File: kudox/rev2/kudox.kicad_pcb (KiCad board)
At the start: 2 copper layers, 143.6 x 129.5 mm, 81 parts, among them K0 KEYSW, K1 KEYSW, K10 KEYSW, K11 KEYSW, K12 KEYSW, K13 KEYSW, K14 KEYSW, K15 KEYSW, K16 KEYSW, K2 KEYSW, K20 KEYSW, K21 KEYSW, K22 KEYSW, K23 KEYSW, K24 KEYSW, K25 KEYSW, K3 KEYSW, K30 KEYSW, K31 KEYSW, K32 KEYSW, K33 KEYSW, K34 KEYSW, K35 KEYSW, K4 KEYSW, K40 KEYSW, K41 KEYSW, K42 KEYSW, K43 KEYSW, K44 KEYSW, K45 KEYSW, K46 KEYSW, K5 KEYSW, U1 ProMicro

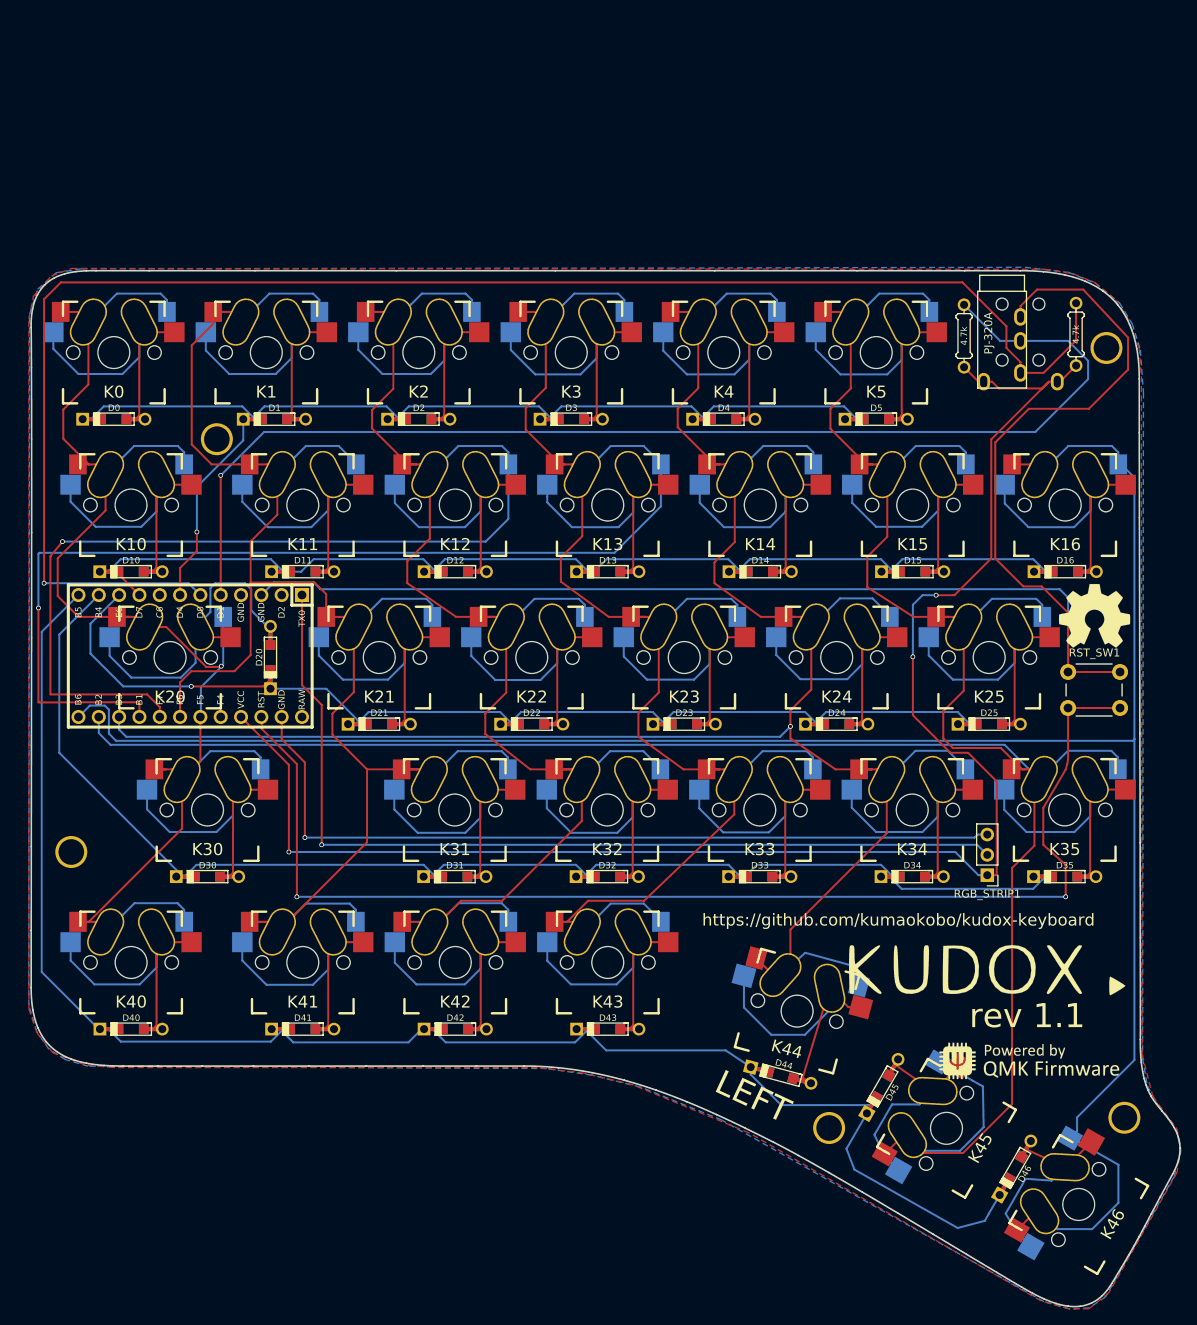
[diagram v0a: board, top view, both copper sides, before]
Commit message: Add more tracks.
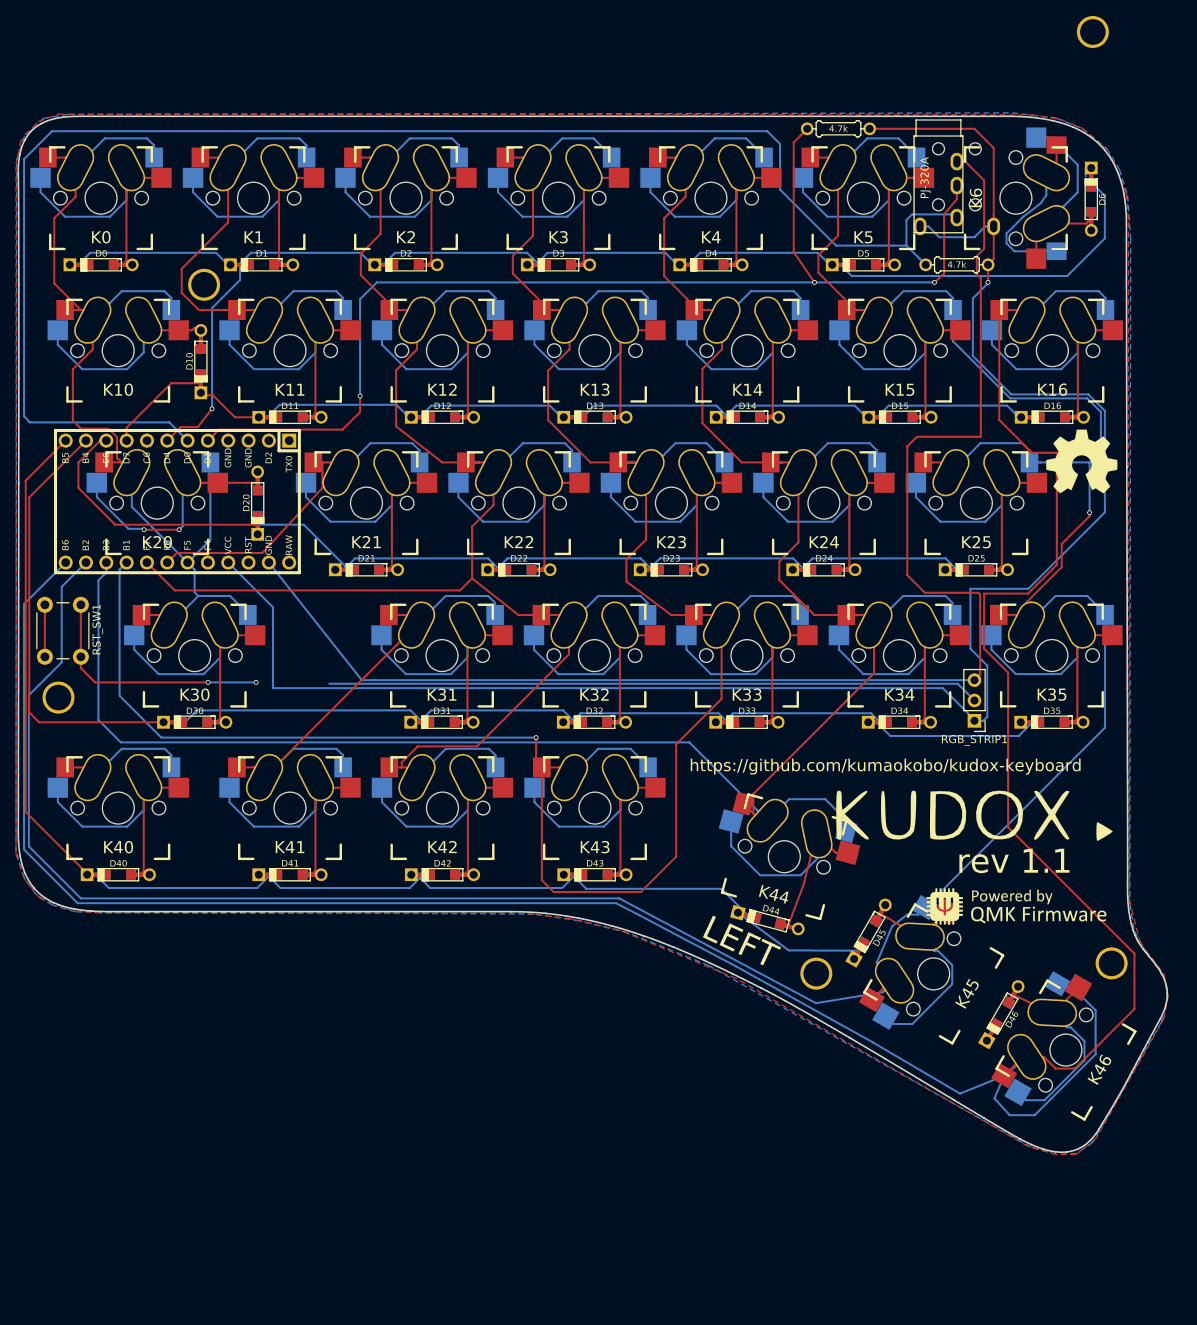
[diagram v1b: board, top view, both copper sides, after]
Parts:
- removed the G*** at (200.4, 138.2)
- removed the G*** at (201.3, 138.1)
- removed the G*** at (206.6, 149.5)
- removed the G*** at (206.8, 149.6)
- removed the HOLE_M3 at (181.5, 157.9)
- removed the HOLE_M3 at (218.4, 156.6)
- removed the HOLE_M3 at (105.0, 71.8)
- removed the HOLE_M3 at (86.8, 123.4)
- removed the HOLE_M3 at (216.2, 60.4)
- added D6: D, kudox_footprints:Diode-dual, F.Cu at (214.3, 41.8)
- added G***: LOGO, kudox_footprints:kudox-logo, B.Cu at (198.8, 118.9)
- added G***: LOGO, kudox_footprints:kudox-logo, F.Cu at (199.7, 118.8)
- added G***: LOGO, myparts:qmk-badge, F.Cu at (205.0, 130.2)
- added G***: LOGO, myparts:qmk-badge, B.Cu at (205.2, 130.3)
- added HOLE_M3: VAL**, keyboard_parts:HOLE_M3, F.Cu at (179.9, 138.6)
- added HOLE_M3: VAL**, keyboard_parts:HOLE_M3, F.Cu at (216.8, 137.3)
- added HOLE_M3: VAL**, keyboard_parts:HOLE_M3, F.Cu at (103.4, 52.5)
- added HOLE_M3: VAL**, keyboard_parts:HOLE_M3, F.Cu at (85.2, 104.1)
- added HOLE_M3: VAL**, keyboard_parts:HOLE_M3, F.Cu at (214.5, 20.9)
- added K6: KEYSW, kudox_footprints:Mx_hotswappable, F.Cu at (204.9, 41.6)
- moved RST_SW1 134.6 mm to (83.5, 99.0), turned to 90 degrees
- moved R1 30.3 mm to (182.7, 33.0), turned to 180 degrees
- moved D10 27.7 mm to (103.0, 62.1), turned to 270 degrees
- moved TRRS1 21.0 mm to (197.5, 33.9)
- moved D46 19.4 mm to (203.2, 143.6)
- moved K45 19.4 mm to (194.6, 138.6)
- moved RGB_STRIP1 19.4 mm to (199.7, 107.0)
- moved D0 19.4 mm to (90.5, 50.0)
- moved D1 19.4 mm to (110.6, 50.0)
- moved D2 19.4 mm to (128.6, 50.0)
- moved D3 19.4 mm to (147.7, 50.0)
- moved D4 19.4 mm to (166.8, 50.0)
- moved D5 19.4 mm to (185.8, 50.0)
- moved -3 19.4 mm to (213.1, 74.6)
- moved D11 19.4 mm to (114.1, 69.0)
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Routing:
- net RST: track 152.6 -> 6.50 mm, vias 2 -> 0
- net col6: track 269.6 -> 371.6 mm
- net GND: track 296.3 -> 209.8 mm, vias 1 -> 2
- net col2: track 289.1 -> 233.6 mm, vias 1 -> 0
- net col1: track 215.5 -> 167.1 mm
- net row0: track 138.8 -> 182.8 mm
- net rgb_data: track 116.0 -> 81.5 mm, vias 1 -> 0
- net VCC: track 202.7 -> 232.9 mm, vias 3 -> 1
- net col0: track 178.9 -> 149.8 mm, vias 1 -> 0
- net row4: track 202.2 -> 174.7 mm
- net Net-(D6-Pad2): track 0.00 -> 27.2 mm
- net col4: track 274.2 -> 298.1 mm, vias 1 -> 0
- net col5: track 351.0 -> 370.7 mm, vias 0 -> 1
- net row1: track 145.5 -> 134.0 mm
- net Net-(D20-Pad2): track 42.5 -> 31.1 mm, vias 0 -> 2
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
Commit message: Modified Mx hotswappable foot print.
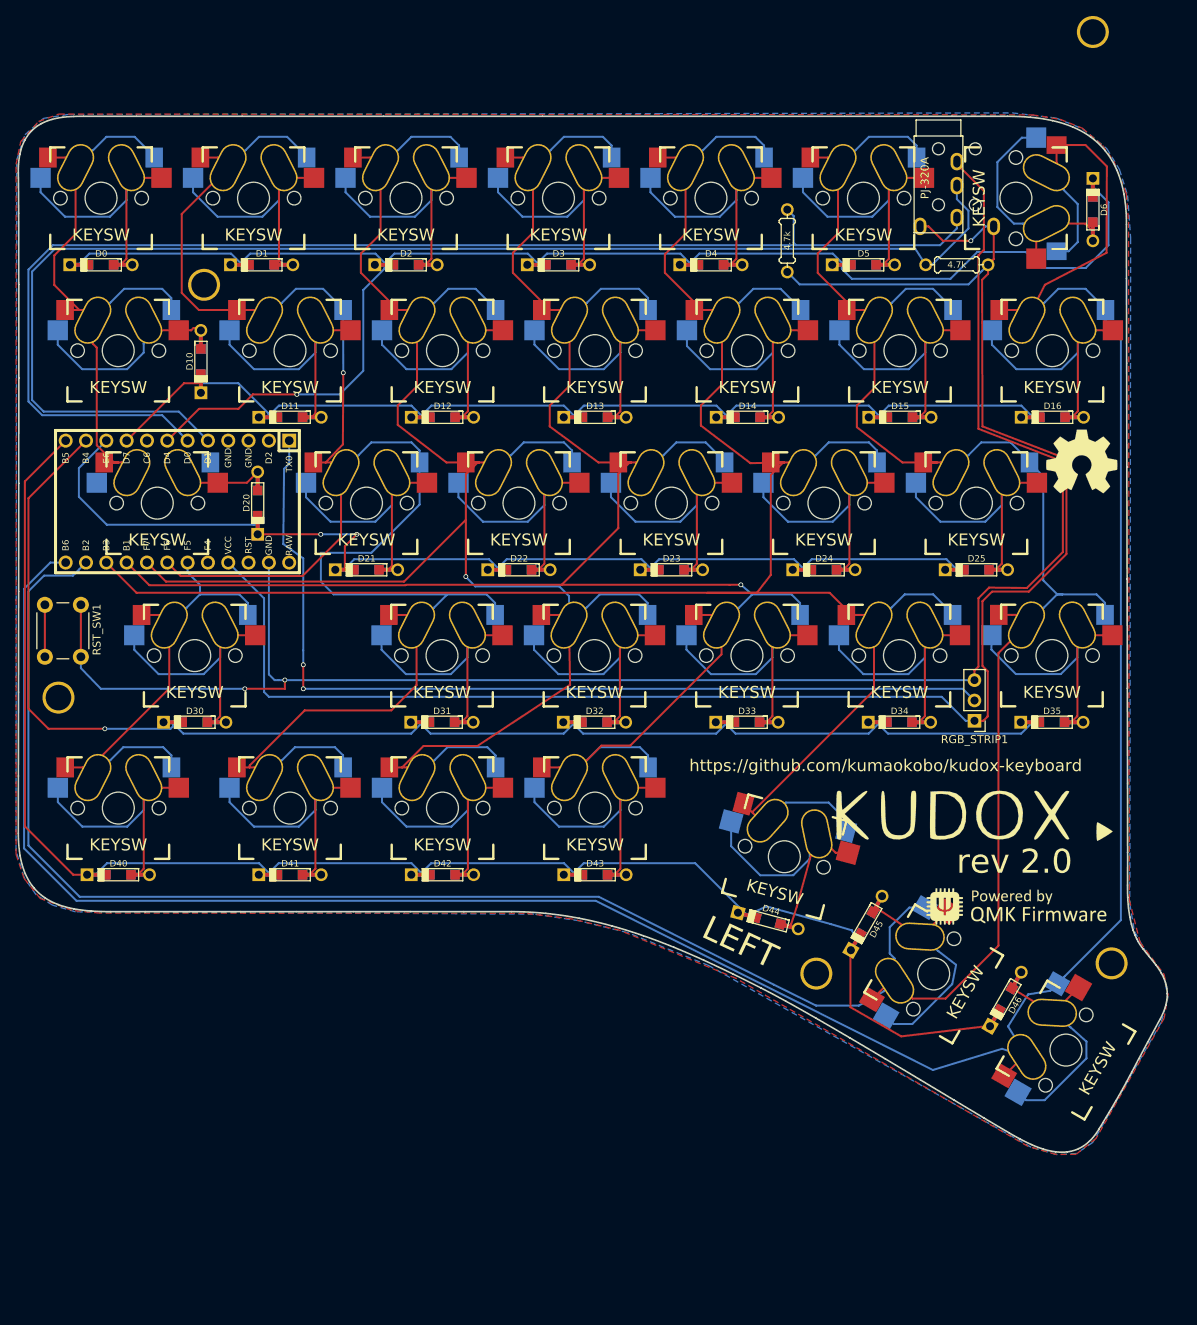
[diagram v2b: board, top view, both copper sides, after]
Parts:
- moved R1 22.5 mm to (197.5, 50.0)
- moved R2 21.4 mm to (176.3, 47.0), turned to 90 degrees
- moved D46 1.84 mm to (203.6, 141.8)
- moved D6 1.32 mm to (214.5, 43.1)
- moved D45 1.17 mm to (186.2, 132.3)
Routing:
- net col1: track 167.1 -> 237.8 mm, vias 0 -> 1
- net col3: track 297.5 -> 261.1 mm
- net rgb_data: track 81.5 -> 117.1 mm, vias 0 -> 2
- net row4: track 174.7 -> 202.6 mm
- net col6: track 371.6 -> 343.8 mm
- net SDA: track 141.2 -> 167.3 mm, vias 3 -> 0
- net SCL: track 188.2 -> 162.8 mm
- net Net-(D20-Pad2): track 31.1 -> 10.5 mm, vias 2 -> 0
- net row0: track 182.8 -> 202.1 mm
- net col4: track 298.1 -> 283.1 mm
- net col0: track 149.8 -> 139.9 mm
- net GND: track 209.8 -> 219.2 mm
- net VCC: track 232.9 -> 224.0 mm
- net col2: track 233.6 -> 241.3 mm, vias 0 -> 1
- net col5: track 370.7 -> 364.4 mm, vias 1 -> 0
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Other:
- board text added: "rev 2.0"
- board text removed: "rev 1.1"

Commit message: Commit on half way.
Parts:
- moved HOLE_M3 29.3 mm to (215.1, 50.2)
- moved R1 21.4 mm to (176.5, 46.1), turned to 90 degrees
- moved R2 19.3 mm to (157.0, 46.1)
- moved D5 6.08 mm to (191.9, 50.0)
- moved TRRS1 2.10 mm to (195.4, 34.0)
- moved D6 1.00 mm to (214.5, 42.1), turned to 270 degrees
- turned K5 to 90 degrees
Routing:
- net col0: track 139.9 -> 195.4 mm, vias 0 -> 3
- net VCC: track 224.0 -> 275.5 mm, vias 1 -> 0
- net RST: track 6.50 -> 40.0 mm, vias 0 -> 1
- net SCL: track 162.8 -> 192.2 mm
- net col1: track 237.8 -> 218.2 mm, vias 1 -> 2
- net Net-(D20-Pad2): track 10.5 -> 29.5 mm
- net col5: track 364.4 -> 355.3 mm
- net row0: track 202.1 -> 193.6 mm
- net col6: track 343.8 -> 348.3 mm
- net Net-(D5-Pad2): track 36.9 -> 32.5 mm
- net SDA: track 167.3 -> 171.6 mm
- net GND: track 219.2 -> 222.9 mm, vias 2 -> 4
- net Net-(D6-Pad2): track 29.8 -> 32.7 mm
- net row2: track 139.6 -> 136.8 mm, vias 2 -> 1
- net row1: track 135.7 -> 136.9 mm
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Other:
- outline, holes or cut-outs redrawn

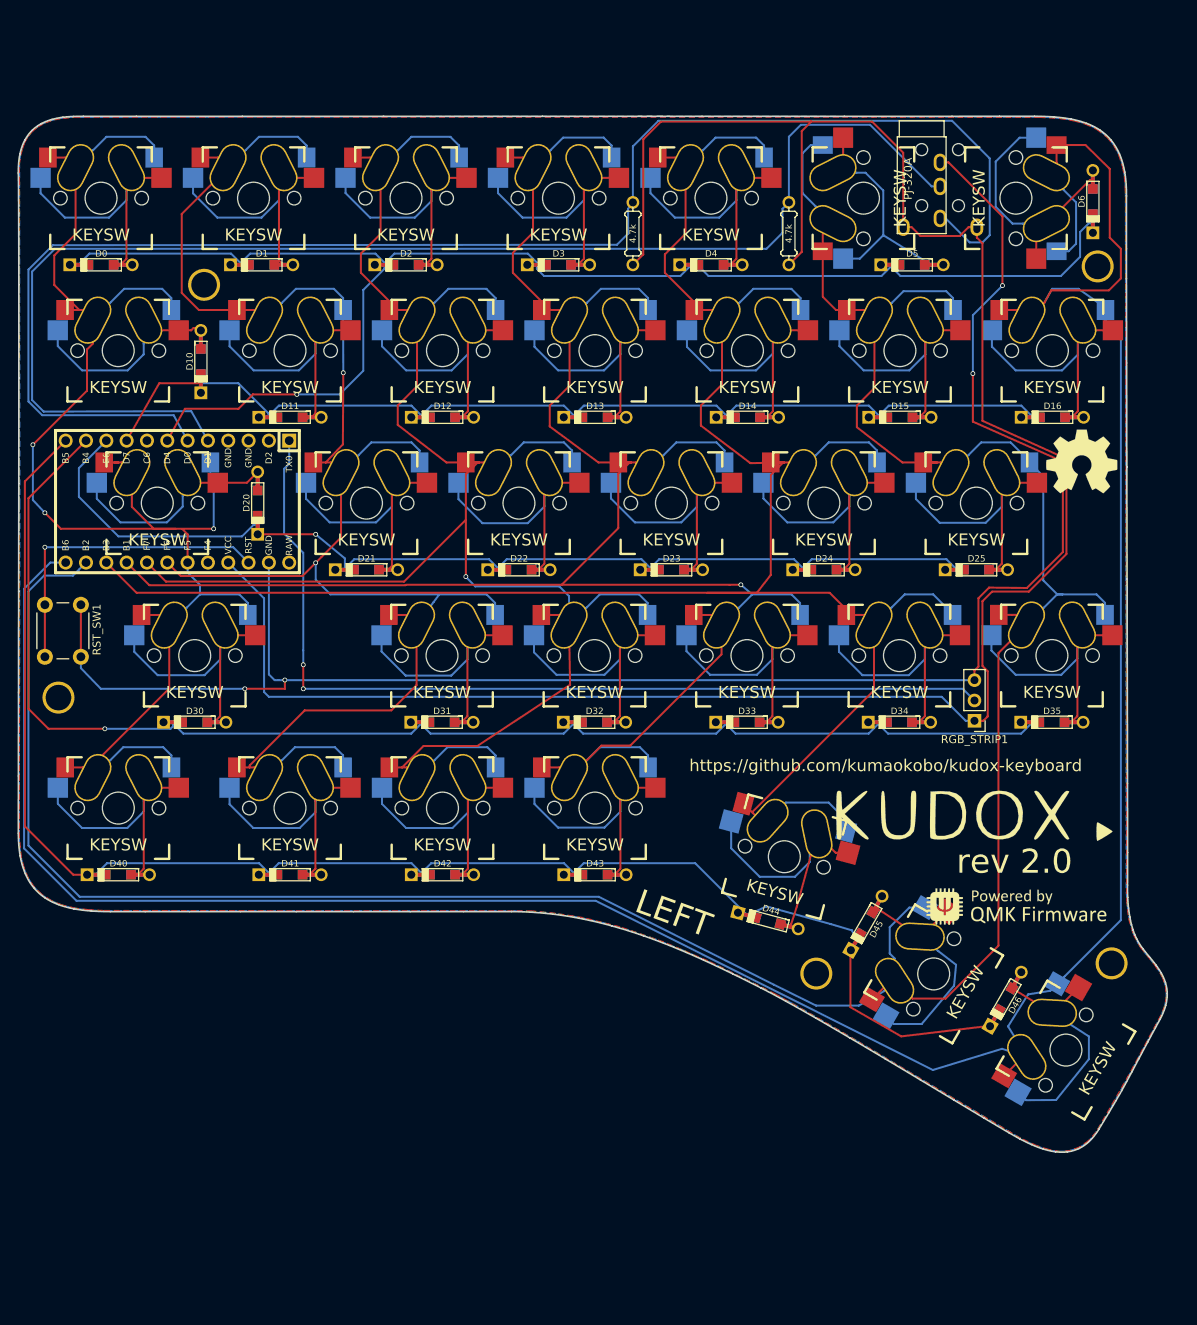
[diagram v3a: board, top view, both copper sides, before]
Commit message: Modified Pro Micro direction.
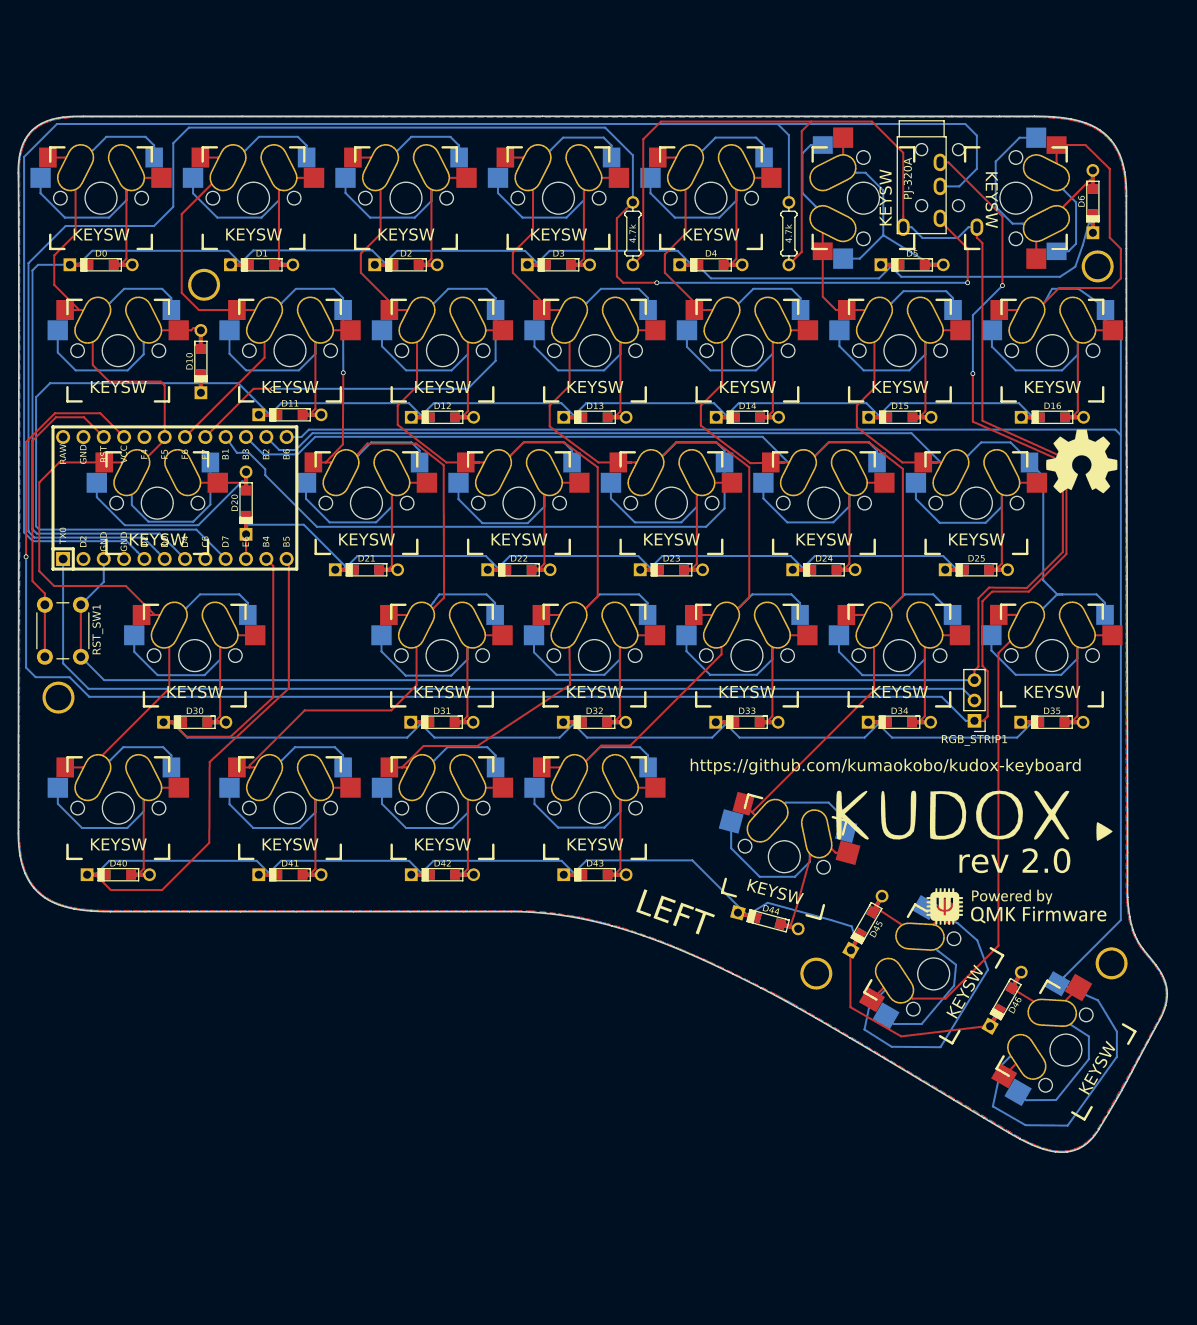
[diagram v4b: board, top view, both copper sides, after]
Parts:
- moved D20 1.45 mm to (108.7, 79.8)
- moved U1 0.55 mm to (99.8, 79.1), turned to 0 degrees
- moved D11 0.31 mm to (114.1, 68.7)
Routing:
- net VCC: track 275.5 -> 331.8 mm, vias 0 -> 1
- net row1: track 136.9 -> 188.1 mm
- net col6: track 348.3 -> 309.8 mm
- net col5: track 355.3 -> 317.1 mm
- net SDA: track 171.6 -> 204.8 mm
- net row2: track 136.8 -> 109.3 mm, vias 1 -> 0
- net row3: track 180.9 -> 160.8 mm, vias 1 -> 0
- net SCL: track 192.2 -> 211.0 mm, vias 0 -> 2
- net row0: track 193.6 -> 210.6 mm, vias 1 -> 0
- net col3: track 261.9 -> 274.3 mm, vias 1 -> 0
- net rgb_data: track 116.8 -> 128.9 mm, vias 2 -> 0
- net GND: track 222.9 -> 211.1 mm, vias 4 -> 2
- net col4: track 284.0 -> 273.9 mm
- net col0: track 195.4 -> 202.9 mm, vias 3 -> 0
- net col2: track 242.3 -> 249.2 mm
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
